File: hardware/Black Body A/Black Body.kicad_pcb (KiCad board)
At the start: 2 copper layers, 55.5 x 53.8 mm, 38 parts, among them IC2 MCP96L00T-E_MX, J1 53307-2471, J2 Conn_01x02, J3 Conn_01x04, J5 Conn_02x04_Top_Bottom, J7 Conn_02x03_Top_Bottom

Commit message: new layout 2.0
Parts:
- removed the R11 at (112.8, 107.5)
- removed the R12 at (112.8, 105.2)
- J3: footprint Connector_Molex:Molex_Nano-Fit_105313-xx04_1x04_P2.50mm_Horizontal -> Connector_PinHeader_2.54mm:PinHeader_1x04_P2.54mm_Vertical
- moved J3 25.8 mm to (104.5, 97.8)
- moved TP_TC_F_2 2.55 mm to (107.5, 99.8)
- moved J2 2.13 mm to (88.5, 105.0)
- moved R11 1.03 mm to (112.2, 109.2)
- moved R12 0.95 mm to (112.2, 111.0)
- moved J7 0.17 mm to (91.0, 84.2)
- moved I2C_SCL1 0.11 mm to (116.5, 92.8)
- renumbered Ra1 to R11, Rb1 to R12
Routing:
- net +3V3: track 50.2 -> 77.1 mm
- net /temp: track 33.4 -> 10.2 mm
- net /INT: track 91.1 -> 78.1 mm
- net /CAN_L: track 33.4 -> 43.1 mm
- net GND: track 7.12 -> 15.6 mm, vias 30 -> 46
- net /I2C1_SDA: track 73.6 -> 66.5 mm, vias 3 -> 1
- net /CAN_H: track 30.7 -> 36.7 mm
- net Net-(IC2-VIN+): track 10.2 -> 13.2 mm
- net /Temp+: track 5.19 -> 7.58 mm
- net /Temp-: track 5.28 -> 7.58 mm
- net Net-(IC2-ADDR): track 2.68 -> 4.60 mm
- net /I2C1_SCL: track 73.5 -> 71.6 mm
- net Net-(Heartbeat1-A): track 0.25 -> 1.96 mm
- net Net-(DB_3-A): track 0.00 -> 1.71 mm
- net Net-(DB_2-A): track 0.00 -> 1.71 mm
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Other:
- board size 55.5 x 53.8 mm -> 52 x 53.8 mm
- board text added: "CAN Conn"
- board text added: "DB1"
- board text added: "DB2"
- board text added: "DB3"
- board text added: "Heartbeat"
- board text added: "Irrad Conn"
- board text added: "ThermoCup Conn"

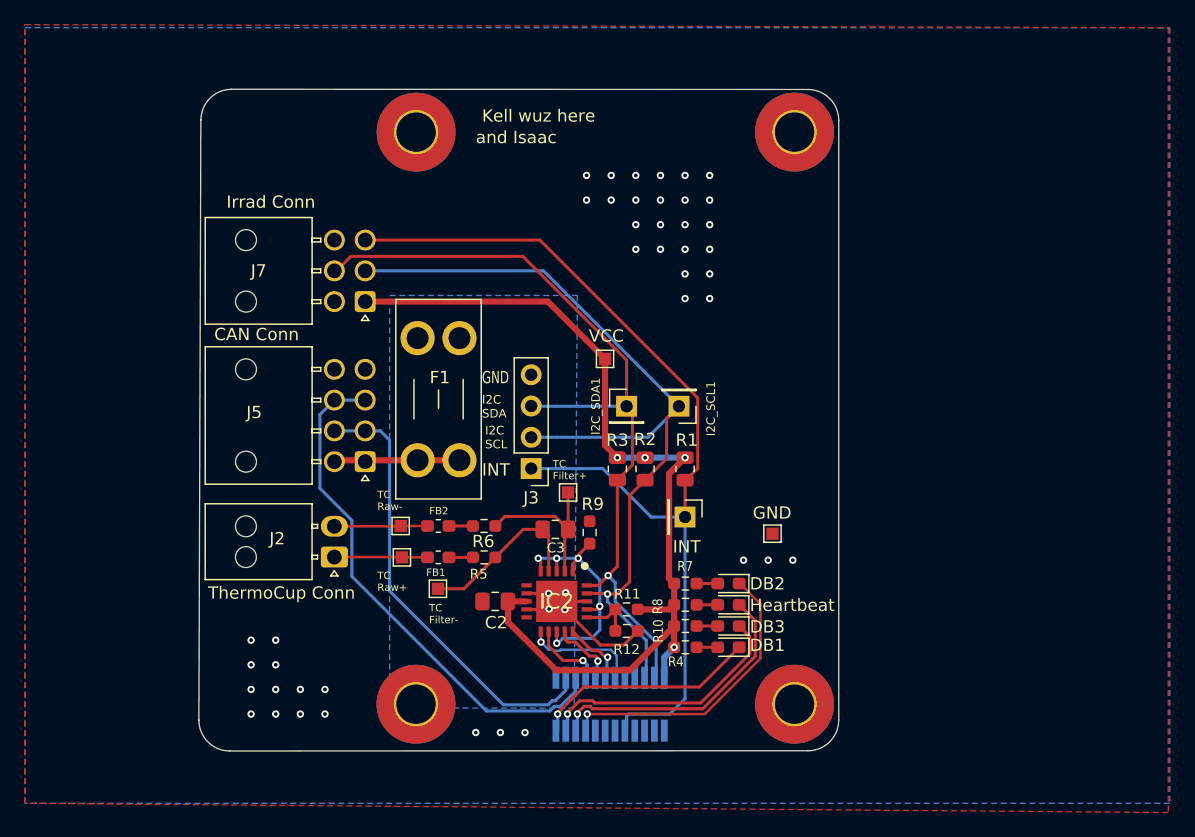
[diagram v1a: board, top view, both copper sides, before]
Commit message: Updated layout and 3D models
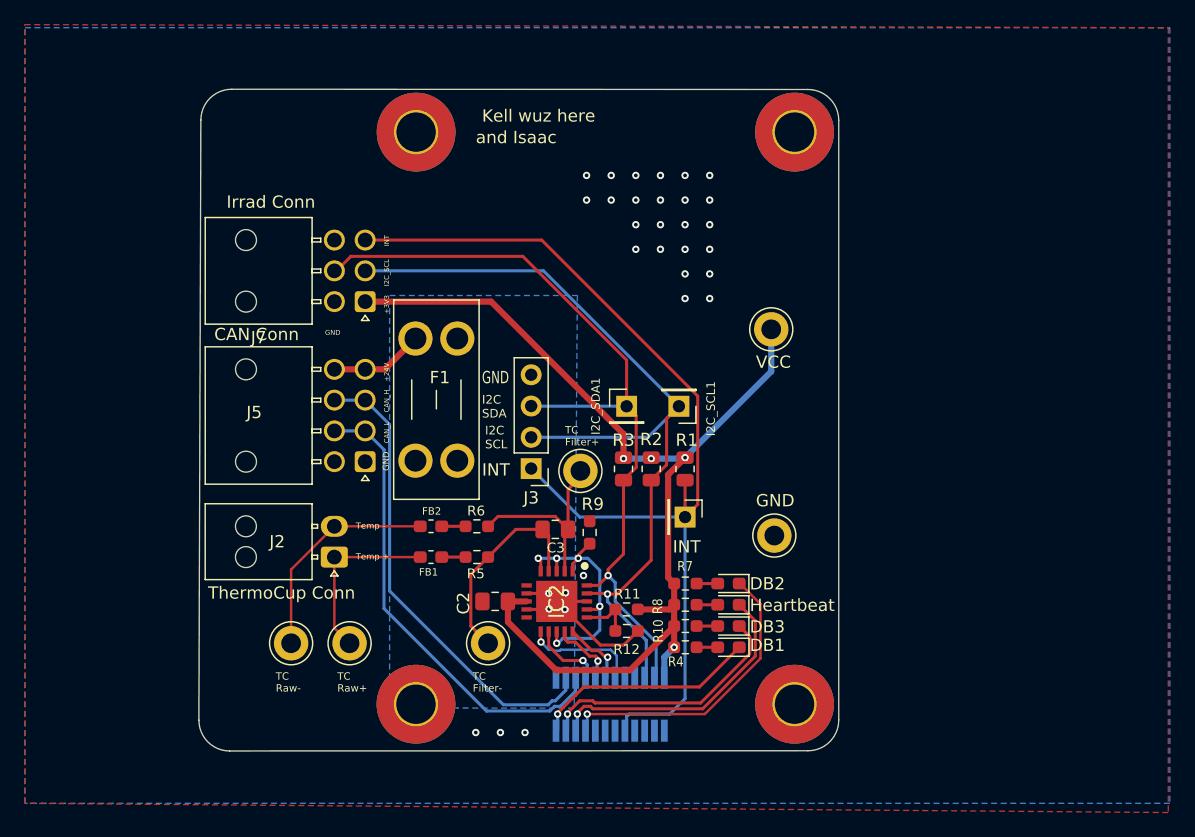
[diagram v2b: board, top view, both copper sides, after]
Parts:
- GND1, TP_TC_1, TP_TC_2, TP_TC_F_1, TP_TC_F_2, VCC1: footprint TestPoint:TestPoint_Pad_1.0x1.0mm -> TestPoint:TestPoint_Keystone_5005-5009_Compact
- IC2: footprint Blackbody Footprint:QFN65P500X500X100-21N-D -> BlackBody:QFN65P500X500X100-21N-D
- J2: footprint Connector_Molex:Molex_Nano-Fit_105313-xx02_1x02_P2.50mm_Horizontal -> utsvt_connectors:105313-2102
- J7: footprint Connector_Molex:Molex_Nano-Fit_105314-xx06_2x03_P2.50mm_Horizontal -> utsvt_connectors:105314-1306
- moved VCC1 13.7 mm to (124.0, 86.5)
- moved TP_TC_2 13.0 mm to (85.0, 112.0)
- moved F2 10.4 mm to (98.5, 87.2), turned to -90 degrees
- moved TP_TC_1 8.17 mm to (89.8, 112.0)
- moved TP_TC_F_1 6.02 mm to (101.0, 112.0)
- moved TP_TC_F_2 2.02 mm to (108.5, 98.0)
- moved FB1 0.59 mm to (96.4, 105.0)
- moved FB2 0.59 mm to (96.4, 102.5)
- moved R5 0.59 mm to (100.1, 105.0)
- moved R6 0.59 mm to (100.1, 102.5)
- moved R2 0.50 mm to (114.2, 97.8)
- moved R3 0.50 mm to (112.0, 97.8)
- moved GND1 0.21 mm to (124.2, 103.2)
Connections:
- F2 pad 1: /temp -> +24V
- J5 pad 1: /temp -> +24V
- J5 pad 5: /temp -> +24V
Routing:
- net +3V3: track 77.1 -> 87.6 mm
- net /Temp-: track 7.58 -> 17.9 mm
- net /temp: track 10.2 -> 0.00 mm
- net +24V: track 0.00 -> 7.62 mm
- net /Temp+: track 7.58 -> 14.5 mm
- net /CAN_L: track 43.1 -> 38.6 mm
- net Net-(IC2-VIN-): track 14.2 -> 17.2 mm
- net Net-(IC2-VIN+): track 13.2 -> 16.2 mm
- net /INT: track 78.1 -> 80.9 mm
- net /CAN_H: track 36.7 -> 38.5 mm
- net GND: track 15.6 -> 15.8 mm, vias 46 -> 32
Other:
- board text added: "+24V"
- board text added: "+3V3"
- board text added: "CAN_H"
- board text added: "CAN_L"
- board text added: "I2C_SCL"
- board text added: "I2C_SDA"
- board text added: "Temp +"
- board text added: "Temp -"
- board text added: "X"
